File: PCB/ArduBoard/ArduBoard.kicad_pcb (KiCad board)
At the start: 2 copper layers, 100.3 x 74.9 mm, 19 parts, among them J1 Conn_01x03_Male, J2 Conn_01x12_Male, J3 Conn_01x02_Male, J4 Conn_01x08_Male, J5 Conn_01x02_Male, J6 Conn_01x02_Male, J7 Conn_01x02_Male, Q1 Q_NMOS_GDS

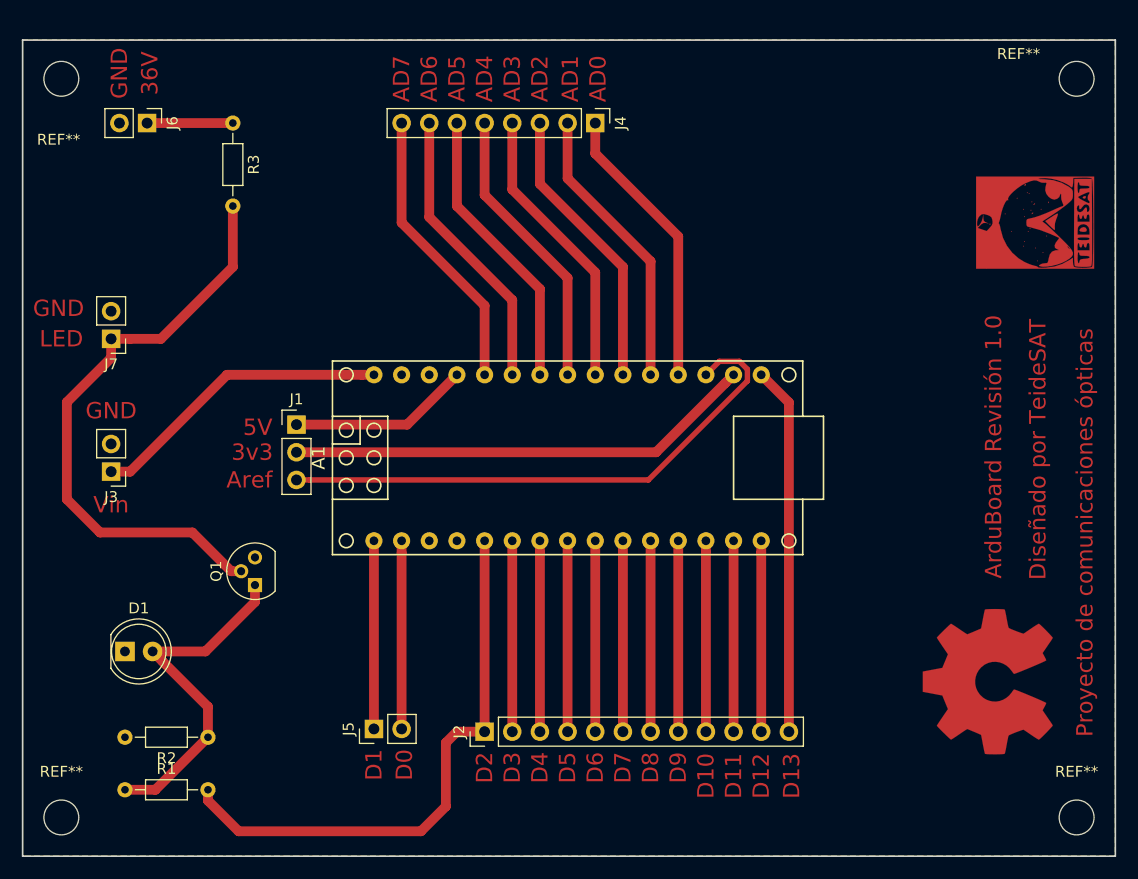
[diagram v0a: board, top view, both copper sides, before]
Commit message: Añadimos el modelo 3D del módulo
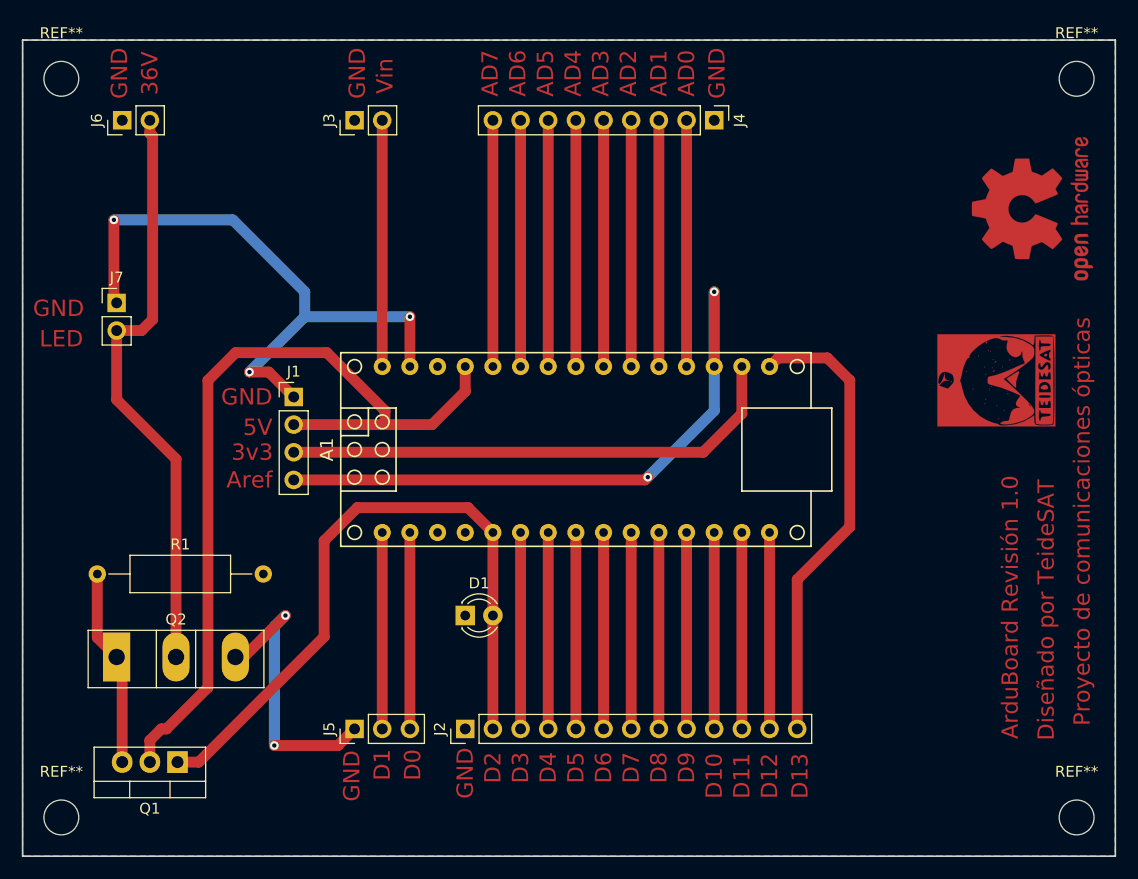
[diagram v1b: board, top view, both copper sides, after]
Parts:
- removed R2: 1k, Resistor_THT:R_Axial_DIN0204_L3.6mm_D1.6mm_P7.62mm_Horizontal
- removed R3: 5, Resistor_THT:R_Axial_DIN0204_L3.6mm_D1.6mm_P7.62mm_Horizontal
- removed the REF** at (182.6, 116.1)
- added Q2: Q_NIGBT_GCE, Package_TO_SOT_THT:TO-247-3_Vertical, F.Cu at (102.6, 113.8)
- added REF**: OSHW-Logo2_14.6x12mm_Copper, Symbol:OSHW-Logo2_14.6x12mm_Copper, F.Cu at (186.7, 72.6)
- D1: footprint LED_THT:LED_D5.0mm -> LED_THT:LED_D3.0mm
- J1: value Conn_01x03_Male -> Conn_01x04_Male; footprint Connector_PinHeader_2.54mm:PinHeader_1x03_P2.54mm_Vertical -> Connector_PinHeader_2.54mm:PinHeader_1x04_P2.54mm_Vertical
- J2: value Conn_01x12_Male -> Conn_01x13_Male; footprint Connector_PinHeader_2.54mm:PinHeader_1x12_P2.54mm_Vertical -> Connector_PinHeader_2.54mm:PinHeader_1x13_P2.54mm_Vertical
- J4: value Conn_01x08_Male -> Conn_01x09_Male; footprint Connector_PinHeader_2.54mm:PinHeader_1x08_P2.54mm_Vertical -> Connector_PinHeader_2.54mm:PinHeader_1x09_P2.54mm_Vertical
- J5: value Conn_01x02_Male -> Conn_01x03_Male; footprint Connector_PinHeader_2.54mm:PinHeader_1x02_P2.54mm_Vertical -> Connector_PinHeader_2.54mm:PinHeader_1x03_P2.54mm_Vertical
- Q1: footprint Package_TO_SOT_THT:TO-92 -> Package_TO_SOT_THT:TO-220-3_Vertical
- R1: value 330 -> 500k; footprint Resistor_THT:R_Axial_DIN0204_L3.6mm_D1.6mm_P7.62mm_Horizontal -> Resistor_THT:R_Axial_DIN0309_L9.0mm_D3.2mm_P15.24mm_Horizontal
- moved J3 39.2 mm to (124.5, 64.5), turned to 90 degrees
- moved D1 31.4 mm to (134.6, 110.0)
- moved R1 20.0 mm to (100.8, 106.2)
- moved Q1 17.7 mm to (108.2, 123.4), turned to 180 degrees
- moved G*** 14.9 mm to (183.4, 88.4)
- moved J4 10.9 mm to (157.5, 64.5)
- moved J7 3.34 mm to (102.6, 81.3), turned to 0 degrees
- moved J1 2.55 mm to (118.9, 89.9)
- moved J6 2.30 mm to (103.1, 64.5), turned to 90 degrees
- moved J2 1.80 mm to (134.6, 120.4)
- moved J5 1.78 mm to (124.5, 120.4)
- moved A1 1.08 mm to (144.8, 94.7)
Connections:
- A1 pad 27: Net-(A1-Pad27) -> 5V
- A1 pad 3: Net-(A1-Pad3) -> (no net)
- D1 pad 2: Net-(D1-Pad2) -> D2
- J1 pad 1: Net-(A1-Pad27) -> GND
- J1 pad 2: Net-(A1-Pad17) -> 5V
- J1 pad 3: Net-(A1-Pad18) -> Net-(A1-Pad17)
- J2 pad 1: D2 -> GND
- J2 pad 10: D11 -> D10
- J2 pad 11: D12 -> D11
- J2 pad 12: D13 -> D12
- J2 pad 2: D3 -> D2
- J2 pad 3: D4 -> D3
- J2 pad 4: D5 -> D4
- J2 pad 5: D6 -> D5
- J2 pad 6: D7 -> D6
- J2 pad 7: D8 -> D7
- J2 pad 8: D9 -> D8
- J2 pad 9: D10 -> D9
- J3 pad 1: Net-(A1-Pad30) -> GND
- J3 pad 2: GND -> Net-(A1-Pad30)
- J4 pad 1: AD0 -> GND
- J4 pad 2: AD1 -> AD0
- J4 pad 3: AD2 -> AD1
- J4 pad 4: AD3 -> AD2
- J4 pad 5: AD4 -> AD3
- J4 pad 6: AD5 -> AD4
- J4 pad 7: AD6 -> AD5
- J4 pad 8: AD7 -> AD6
- J5 pad 1: D1 -> GND
- J5 pad 2: D0 -> D1
- J6 pad 1: 36V -> GND
- J6 pad 2: GND -> 36V
- J7 pad 1: LED_LOAD -> GND
- J7 pad 2: GND -> 36V
- Q1 pad 1: Net-(D1-Pad2) -> D2
- Q1 pad 2: LED_LOAD -> 5V
- Q1 pad 3: GND -> CONTROL
- R1 pad 1: Net-(D1-Pad2) -> CONTROL
- R1 pad 2: D2 -> GND
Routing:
- net GND: track 0.00 -> 83.2 mm, vias 0 -> 5
- net 5V: track 0.00 -> 77.6 mm
- net LED_LOAD: track 54.7 -> 0.00 mm
- net 36V: track 7.87 -> 54.3 mm
- net Net-(D1-Pad2): track 32.4 -> 0.00 mm
- net CONTROL: track 0.00 -> 18.2 mm
- net Net-(A1-Pad27): track 16.6 -> 0.00 mm
- net D2: track 52.3 -> 62.8 mm
- net D13: track 33.8 -> 42.5 mm
- net Net-(A1-Pad18): track 50.9 -> 59.0 mm, vias 0 -> 2
- net Net-(A1-Pad30): track 27.8 -> 22.6 mm
- net Net-(A1-Pad17): track 43.1 -> 46.9 mm
- net AD2: track 26.3 -> 22.6 mm
- net AD7: track 26.3 -> 22.6 mm
- net AD5: track 26.3 -> 22.6 mm
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
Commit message: Añadimos la versión corregida de la PCB (pistas en TOP y BOT)
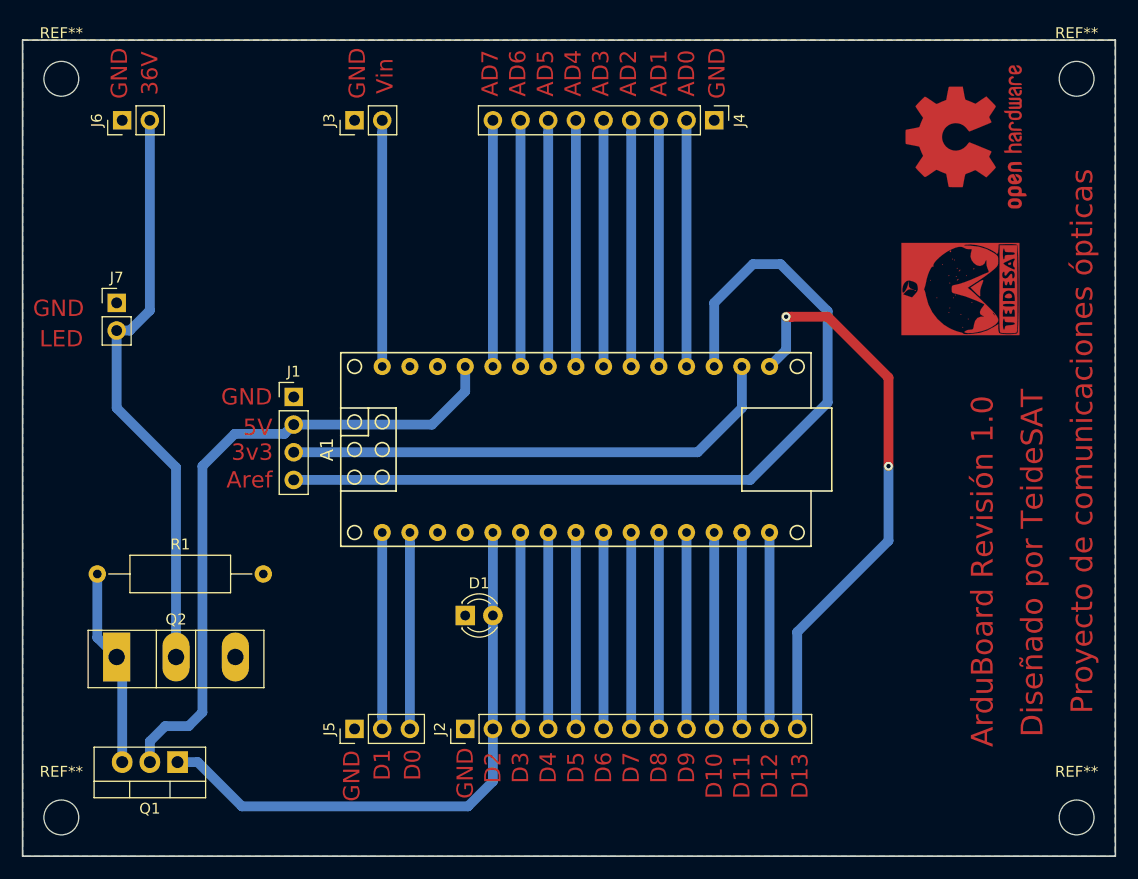
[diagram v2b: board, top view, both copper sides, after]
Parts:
- moved G*** 9.01 mm to (180.1, 80.0)
- moved REF** 8.99 mm to (180.6, 66.0)
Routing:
- net GND: track 83.2 -> 0.00 mm, vias 5 -> 0
- net Net-(A1-Pad18): track 59.0 -> 79.9 mm, vias 2 -> 0
- net 5V: track 77.6 -> 59.7 mm
- net D13: track 42.5 -> 52.6 mm, vias 0 -> 2
- net D2: track 62.8 -> 54.4 mm
- net 36V: track 54.3 -> 53.5 mm
- added copper zone on B.Cu, net GND

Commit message: Añadimos la versión para la fabricación en la ProtoMat
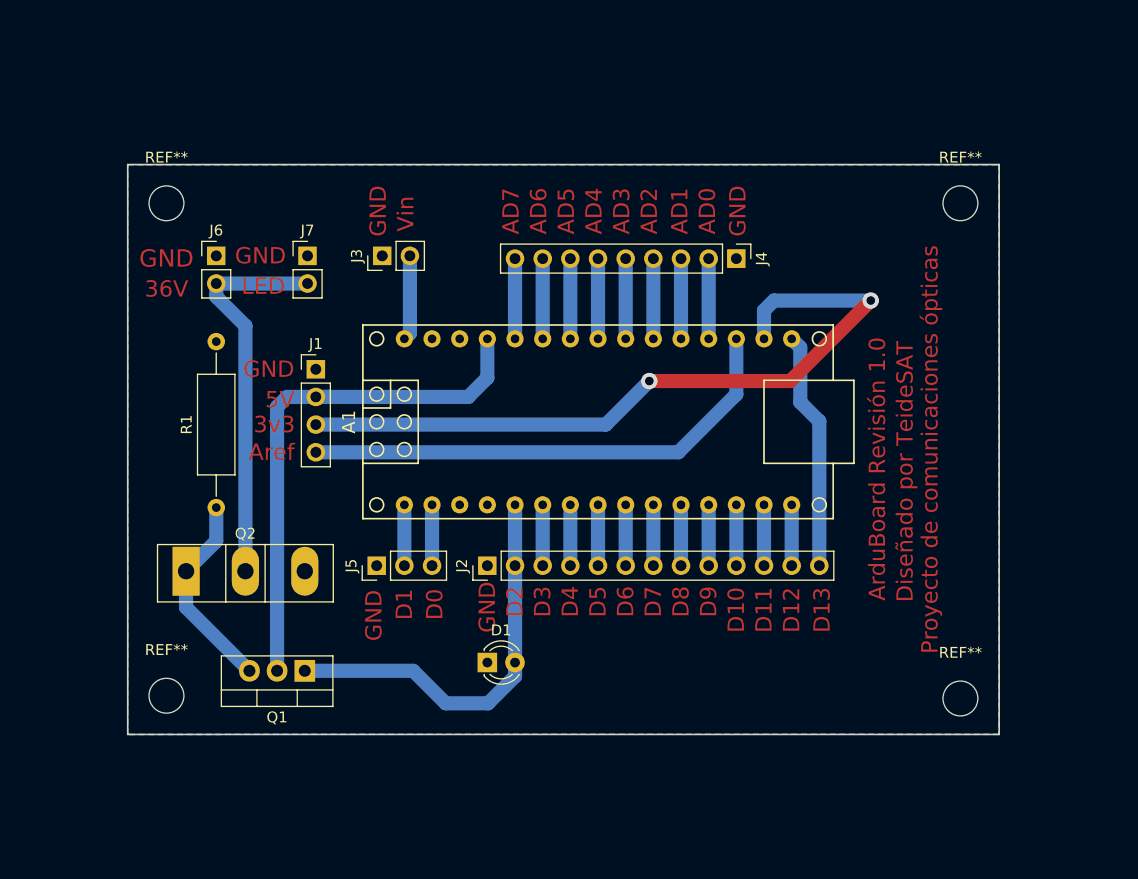
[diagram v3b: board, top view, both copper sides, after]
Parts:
- removed G***: LOGO, Librerias:Logo_TeideSat
- removed the REF** at (180.6, 66.0)
- moved REF** 84.3 mm to (107.2, 72.1)
- moved REF** 83.3 mm to (180.1, 117.6)
- moved REF** 57.5 mm to (107.2, 117.3)
- moved REF** 57.4 mm to (180.1, 72.1)
- moved J7 18.1 mm to (120.1, 77.0)
- moved J6 15.1 mm to (111.8, 77.0), turned to 0 degrees
- moved J5 15.1 mm to (126.5, 105.4)
- moved J2 15.1 mm to (136.7, 105.4)
- moved Q1 14.4 mm to (119.9, 115.1)
- moved J4 12.9 mm to (159.5, 77.2)
- moved J3 12.7 mm to (127.0, 77.0)
- moved R1 12.5 mm to (111.8, 100.1), turned to 90 degrees
- moved Q2 10.1 mm to (109.0, 105.9)
- moved D1 4.77 mm to (136.7, 114.3)
- moved A1 3.25 mm to (146.8, 92.2)
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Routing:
- net Net-(A1-Pad18): track 79.9 -> 45.9 mm
- net D13: track 52.6 -> 21.9 mm, vias 2 -> 0
- net Net-(A1-Pad17): track 46.6 -> 68.5 mm, vias 0 -> 2
- net 36V: track 53.5 -> 35.9 mm
- net D2: track 54.4 -> 37.3 mm
- net AD7: track 22.6 -> 7.37 mm
- net AD6: track 22.6 -> 7.37 mm
- net AD5: track 22.6 -> 7.37 mm
- net AD4: track 22.6 -> 7.37 mm
- net AD3: track 22.6 -> 7.37 mm
- net AD2: track 22.6 -> 7.37 mm
- net AD1: track 22.6 -> 7.37 mm
- net AD0: track 22.6 -> 7.37 mm
- net Net-(A1-Pad30): track 22.6 -> 7.83 mm
- net D9: track 18.0 -> 5.59 mm
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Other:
- board size 100.3 x 74.9 mm -> 80 x 52.3 mm
